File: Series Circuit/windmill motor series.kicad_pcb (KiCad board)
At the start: 2 copper layers, 9 parts

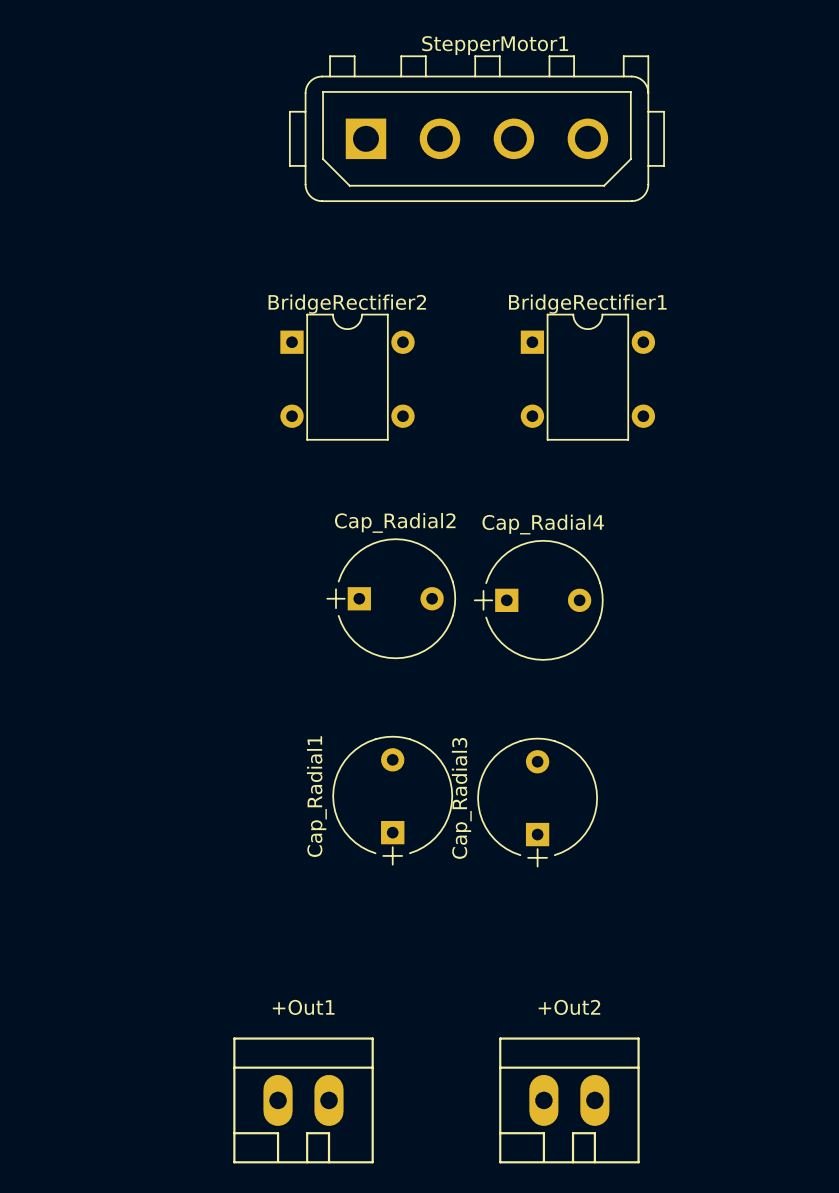
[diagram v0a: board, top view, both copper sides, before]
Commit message: Separate out power flags and add jumpers to allow tied operation.
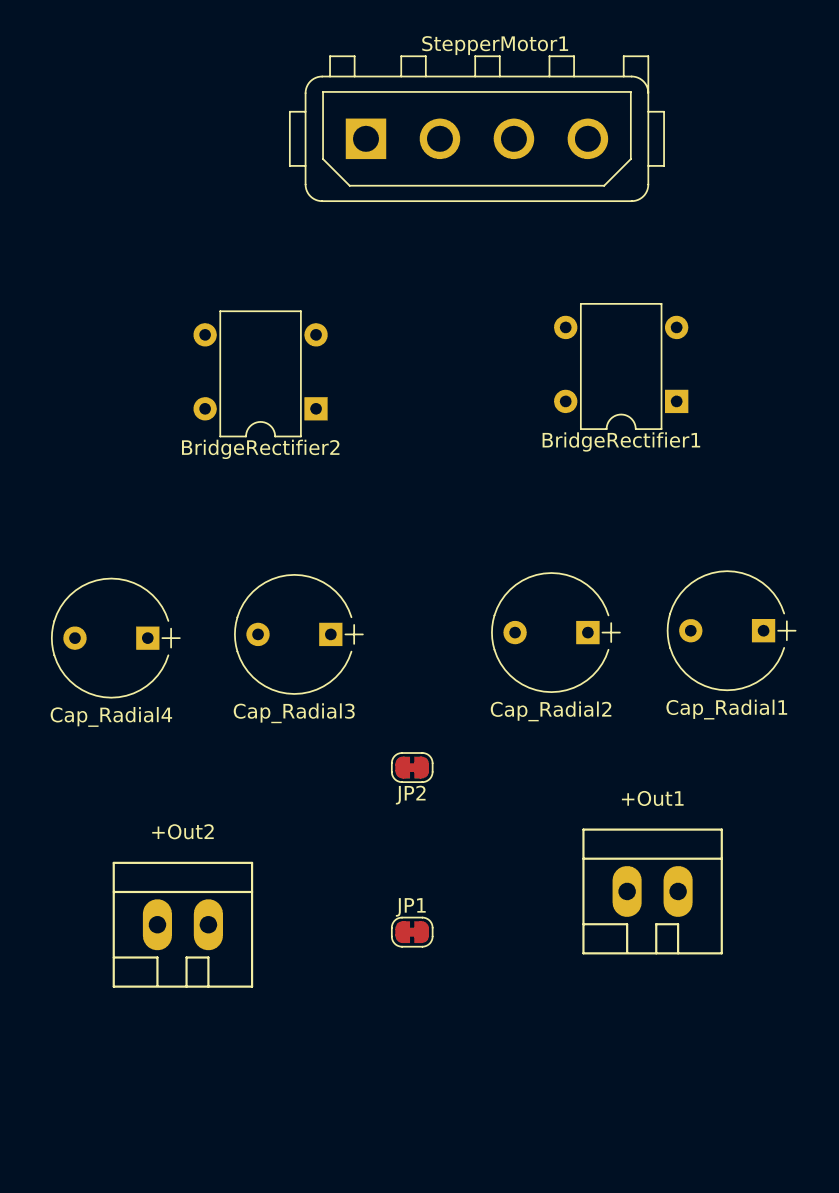
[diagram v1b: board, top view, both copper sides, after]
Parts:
- added JP1: +ve tie, Jumper:SolderJumper-2_P1.3mm_Bridged_RoundedPad1.0x1.5mm, F.Cu at (89.5, 104.0)
- added JP2: -ve tie, Jumper:SolderJumper-2_P1.3mm_Bridged_RoundedPad1.0x1.5mm, F.Cu at (89.5, 92.7)
- moved +Out2 29.2 mm to (73.8, 103.5)
- moved Cap_Radial1 29.0 mm to (113.7, 83.3), turned to 180 degrees
- moved +Out1 27.9 mm to (106.0, 101.2)
- moved Cap_Radial4 24.8 mm to (71.4, 83.8), turned to 180 degrees
- moved Cap_Radial3 19.8 mm to (83.9, 83.6), turned to 180 degrees
- moved Cap_Radial2 15.9 mm to (101.6, 83.4), turned to 180 degrees
- moved BridgeRectifier1 10.7 mm to (107.7, 67.6), turned to 180 degrees
- moved BridgeRectifier2 4.86 mm to (82.9, 68.1), turned to 180 degrees
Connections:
- +Out1 pad 1: GND -> GND1
- +Out1 pad 2: +12V -> VCC
- +Out2 pad 1: GND -> GND2
- +Out2 pad 2: +12V -> VDD
- BridgeRectifier1 pad 1: +12V -> VCC
- BridgeRectifier1 pad 4: GND -> GND1
- BridgeRectifier2 pad 1: +12V -> VDD
- BridgeRectifier2 pad 4: GND -> GND2
- Cap_Radial1 pad 1: +12V -> VCC
- Cap_Radial2 pad 2: GND -> GND1
- Cap_Radial3 pad 1: +12V -> VDD
- Cap_Radial4 pad 2: GND -> GND2
